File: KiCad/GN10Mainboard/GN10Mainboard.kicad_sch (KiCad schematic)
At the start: 140 parts, among them J1 XT30PW-M, J10 USB_C_Receptacle_USB2.0, J12 Conn_01x04, J4 Conn_01x04, J5 Conn_01x06, J6 Conn_01x04, J7 Conn_01x04, J8 Conn_01x04, J9 RJ45_Bel_SI-60062-F, SW1 SW_Push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

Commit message: update
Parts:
- L3: value 7.2u -> 6.8u
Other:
- note removed: "Virtual COM port allows communication to both STM32 and ESP32 Port A connects to STM, port B to ESP Refer to datasheet for details"
- moved on the sheet: C1, C10, C11, C19, C20, C21, C22, C23, C24, C25, C28, C29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

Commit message: add:footprint
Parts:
- C1, C13, C14, C15: footprint (none) -> Capacitor_SMD:C_0402_1005Metric
- C16, C17, C18, C2, C26: footprint (none) -> Capacitor_SMD:C_1210_3225Metric
- D2: footprint (none) -> Diode_SMD:D_SMC
- JP1, JP2: footprint (none) -> Jumper:SolderJumper-2_P1.3mm_Open_RoundedPad1.0x1.5mm
- L3: footprint (none) -> Inductor_SMD:L_Bourns_SRR1210A
- R11, R12, R13, R14, R2, R3, R4, R40, R41, R42, R43: footprint (none) -> Resistor_SMD:R_0402_1005Metric
- U3: footprint (none) -> Package_SO:SOIC-8_3.9x4.9mm_P1.27mm
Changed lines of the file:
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@@
 			)
 		)
-		(property "Footprint" ""
+		(property "Footprint" "Resistor_SMD:R_0402_1005Metric"
 			(at 88.392 350.52 90)
 			(effects
@@
 			)
 		)
-		(property "Footprint" ""
+		(property "Footprint" "Jumper:SolderJumper-2_P1.3mm_Open_RoundedPad1.0x1.5mm"
 			(at 203.2 293.37 0)
 			(effects
@@
 			)
 		)
-		(property "Footprint" ""
+		(property "Footprint" "Resistor_SMD:R_0402_1005Metric"
 			(at 257.302 73.66 90)
 			(effects
@@
 			)
 		)
-		(property "Footprint" ""
+		(property "Footprint" "Resistor_SMD:R_0402_1005Metric"
 			(at 159.512 80.01 90)
 			(effects
@@
 			)
 		)
-		(property "Footprint" ""
+		(property "Footprint" "Resistor_SMD:R_0402_1005Metric"
 			(at 257.302 85.09 90)
 			(effects
@@
 			)
 		)
-		(property "Footprint" ""
+		(property "Footprint" "Package_SO:SOIC-8_3.9x4.9mm_P1.27mm"
 			(at 74.93 361.95 0)
 			(effects
@@
 			)
 		)
-		(property "Footprint" ""
+		(property "Footprint" "Resistor_SMD:R_0402_1005Metric"
 			(at 96.012 350.52 90)
 			(effects
@@
 			)
 		)
-		(property "Footprint" ""
+		(property "Footprint" "Resistor_SMD:R_0402_1005Metric"
 			(at 103.632 350.52 90)
 			(effects
@@
 			)
 		)
-		(property "Footprint" ""
+		(property "Footprint" "Resistor_SMD:R_0402_1005Metric"
 			(at 121.412 80.01 90)
 			(effects
@@
 			)
 		)
-		(property "Footprint" ""
+		(property "Footprint" "Capacitor_SMD:C_1210_3225Metric"
 			(at 233.3752 74.93 0)
 			(effects
@@
 			)
 		)
-		(property "Footprint" ""
+		(property "Footprint" "Capacitor_SMD:C_1210_3225Metric"
 			(at 97.4852 69.85 0)
 			(effects
@@
 			)
 		)
-		(property "Footprint" ""
+		(property "Footprint" "Diode_SMD:D_SMC"
 			(at 201.93 71.12 0)
 			(effects
@@
 			)
 		)
-		(property "Footprint" ""
+		(property "Footprint" "Inductor_SMD:L_Bourns_SRR1210A"
 			(at 212.09 67.31 0)
 			(effects
@@
 			)
 		)
-		(property "Footprint" ""
+		(property "Footprint" "Capacitor_SMD:C_0402_1005Metric"
 			(at 56.8452 361.95 0)
 			(effects
@@
 			)
 		)
-		(property "Footprint" ""
+		(property "Footprint" "Capacitor_SMD:C_0402_1005Metric"
 			(at 138.1252 81.28 0)
 			(effects
@@
 			)
 		)
-		(property "Footprint" ""
+		(property "Footprint" "Resistor_SMD:R_0402_1005Metric"
 			(at 194.31 295.148 90)
 			(effects
@@
 			)
 		)
-		(property "Footprint" ""
+		(property "Footprint" "Capacitor_SMD:C_1210_3225Metric"
 			(at 244.8052 74.93 0)
 			(effects
@@
 			)
 		)
-		(property "Footprint" ""
+		(property "Footprint" "Capacitor_SMD:C_0402_1005Metric"
 			(at 195.2752 67.31 0)
 			(effects
@@
 			)
 		)
-		(property "Footprint" ""
+		(property "Footprint" "Resistor_SMD:R_0402_1005Metric"
 			(at 121.412 66.04 90)
 			(effects
@@
 			)
 		)
-		(property "Footprint" ""
+		(property "Footprint" "Capacitor_SMD:C_0402_1005Metric"
 			(at 148.2852 85.09 0)
 			(effects
@@
 			)
 		)
-		(property "Footprint" ""
+		(property "Footprint" "Jumper:SolderJumper-2_P1.3mm_Open_RoundedPad1.0x1.5mm"
 			(at 203.2 290.83 0)
 			(effects
@@
 			)
 		)
-		(property "Footprint" ""
+		(property "Footprint" "Resistor_SMD:R_0402_1005Metric"
 			(at 145.542 73.66 90)
 			(effects
@@
 			)
 		)
-		(property "Footprint" ""
+		(property "Footprint" "Capacitor_SMD:C_1210_3225Metric"
 			(at 108.9152 69.85 0)
 			(effects
@@
 			)
 		)
-		(property "Footprint" ""
+		(property "Footprint" "Capacitor_SMD:C_1210_3225Metric"
 			(at 221.9452 74.93 0)
 			(effects
@@
 			)
 		)
-		(property "Footprint" ""
+		(property "Footprint" "Resistor_SMD:R_0402_1005Metric"
 			(at 101.6 366.268 90)
 			(effects

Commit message: update
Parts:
- added J11, J2, J3: Conn_01x04, Connector_JST:JST_XH_B4B-XH-A_1x04_P2.50mm_Vertical, symbol Connector_Generic:Conn_01x04
- added J13, J14: Conn_01x06, Connector_JST:JST_XH_B6B-XH-A_1x06_P2.50mm_Vertical, symbol Connector_Generic:Conn_01x06
- added R44, R45, R46: 120, Resistor_SMD:R_0402_1005Metric, symbol Device:R
- R43: value 330 -> 470
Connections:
- net +3.3V: now also J13.2 (Pin_2), J14.2 (Pin_2)
- net +5V: now also J11.3 (Pin_3), J2.3 (Pin_3), J3.3 (Pin_3)
- net CAN1_H: now also J2.4 (Pin_4), R44.1
- net CAN1_L: now also J2.2 (Pin_2), R44.2
- net CAN2_H: now also J3.4 (Pin_4), R45.1
- net CAN2_L: now also J3.2 (Pin_2), R45.2
- net CAN3_H: now also J11.4 (Pin_4), R46.1
- net CAN3_L: now also J11.2 (Pin_2), R46.2
- net GND: now also J11.1 (Pin_1), J13.4 (Pin_4), J14.4 (Pin_4), J2.1 (Pin_1), J3.1 (Pin_1)
- net TIM3_CH1: now also J14.1 (Pin_1); no longer J5.6 (Pin_6)
- net TIM3_CH2: now also J14.3 (Pin_3); no longer J5.5 (Pin_5)
- net TIM2_CH1: now reaches U4.12 (PA0)
- net TIM2_CH1: now also J13.1 (Pin_1)
- net TIM2_CH2: now reaches U4.13 (PA1)
- net TIM2_CH2: now also J13.3 (Pin_3)
- no-connect marks 53 -> 57
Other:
- note added: "+5V max current : 5A"
- note added: "BATT : 7.2-24V"
- note added: "Switch"
- note removed: "BATT : 7-14V"
- note removed: "External-Switch"
- moved on the sheet: C13, C14, C15, C16, C17, C18, C19, C2, C20, C21, C22, C23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

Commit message: add:Jetson connectors
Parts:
- added C27, C41: 0.1u, Capacitor_SMD:C_0402_1005Metric, symbol Device:C
- added D8: White, LED_SMD:LED_0603_1608Metric, symbol Device:LED
- added J15: Conn_01x12, symbol Connector_Generic:Conn_01x12
- added J16: Conn_01x04, symbol Connector_Generic:Conn_01x04
- added J17: Conn_01x04, Connector_JST:JST_XH_B4B-XH-A_1x04_P2.50mm_Vertical, symbol Connector_Generic:Conn_01x04
- added JP3, JP4: Jumper_2_Small_Open, Jumper:SolderJumper-2_P1.3mm_Open_RoundedPad1.0x1.5mm, symbol Jumper:Jumper_2_Small_Open
- added R47: 120, Resistor_SMD:R_0402_1005Metric, symbol Device:R
- added U11: MCP2562-E-SN, Package_SO:SOIC-8_3.9x4.9mm_P1.27mm, symbol Interface_CAN_LIN:MCP2562-E-SN
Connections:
- net +5V: now also C41.1, J17.3 (Pin_3), U11.3 (VDD)
- net GND: now also C27.2, C41.2, J15.11 (Pin_11), J15.7 (Pin_7), J15.9 (Pin_9), J16.3 (Pin_3), J17.1 (Pin_1), U11.2 (VSS), U11.8 (STBY)
- net SYS_SWDIO: now also U9.18 (ADBUS2)
- net at JP2.1 (A), R43.1: now also JP4.1 (A); no longer U9.18 (ADBUS2)
- net at JP1.1 (A), U9.16 (ADBUS0): now also JP3.1 (A)
- new net JETSON_3.3V: C27.1, J16.4 (Pin_4), U11.5 (Vio)
- new net JETSON_CAN_H: J17.4 (Pin_4), R47.1, U11.7 (CANH)
- new net JETSON_CAN_L: J17.2 (Pin_2), R47.2, U11.6 (CANL)
- new net JETSON_CAN_RX: J16.2 (Pin_2), U11.4 (RXD)
- new net JETSON_CAN_TX: J16.1 (Pin_1), U11.1 (TXD)
- new net JETSON_PC_LED+: D8.2 (A), J15.2 (Pin_2)
- new net JETSON_PC_LED-: D8.1 (K), J15.1 (Pin_1)
- new net JETSON_UART2_RXD: J15.3 (Pin_3), JP4.2 (B)
- new net JETSON_UART2_TXD: J15.4 (Pin_4), JP3.2 (B)
- no-connect marks 57 -> 62
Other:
- moved on the sheet: JP1, JP2

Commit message: remove:jetson connectors
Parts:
- removed C27, C41: 0.1u, Capacitor_SMD:C_0402_1005Metric, symbol Device:C
- removed D8: White, LED_SMD:LED_0603_1608Metric, symbol Device:LED
- removed J15: Conn_01x12, symbol Connector_Generic:Conn_01x12
- removed J16: Conn_01x04, symbol Connector_Generic:Conn_01x04
- removed J17: Conn_01x04, Connector_JST:JST_XH_B4B-XH-A_1x04_P2.50mm_Vertical, symbol Connector_Generic:Conn_01x04
- removed JP3, JP4: Jumper_2_Small_Open, Jumper:SolderJumper-2_P1.3mm_Open_RoundedPad1.0x1.5mm, symbol Jumper:Jumper_2_Small_Open
- removed R47: 120, Resistor_SMD:R_0402_1005Metric, symbol Device:R
- removed U11: MCP2562-E-SN, Package_SO:SOIC-8_3.9x4.9mm_P1.27mm, symbol Interface_CAN_LIN:MCP2562-E-SN
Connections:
- net SYS_SWDIO: no longer U9.18 (ADBUS2)
- net at JP2.1 (A), R43.1: now also U9.18 (ADBUS2)
- no-connect marks 62 -> 57

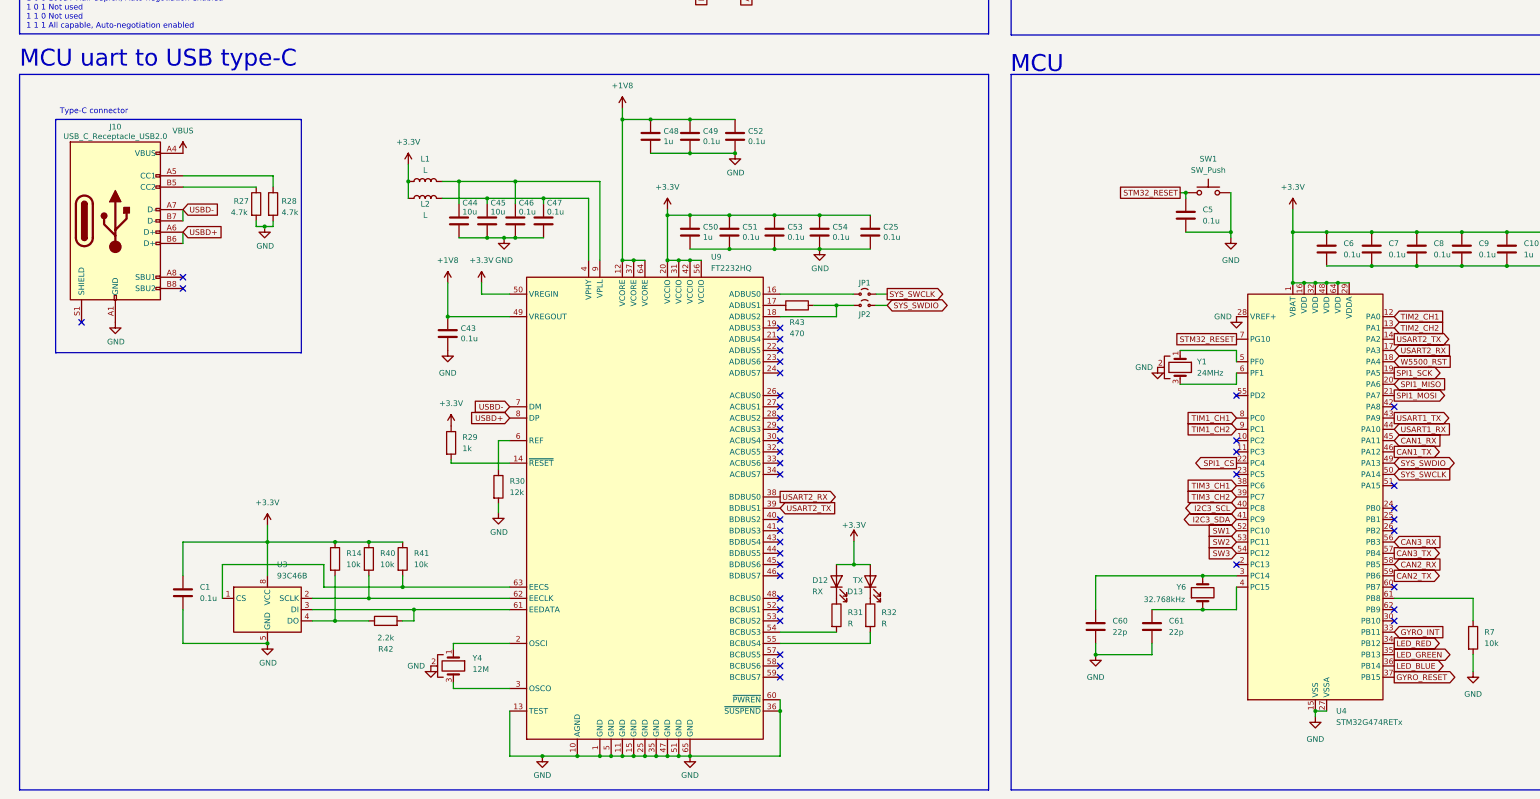
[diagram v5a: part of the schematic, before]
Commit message: update:Serial conv to ft231xs
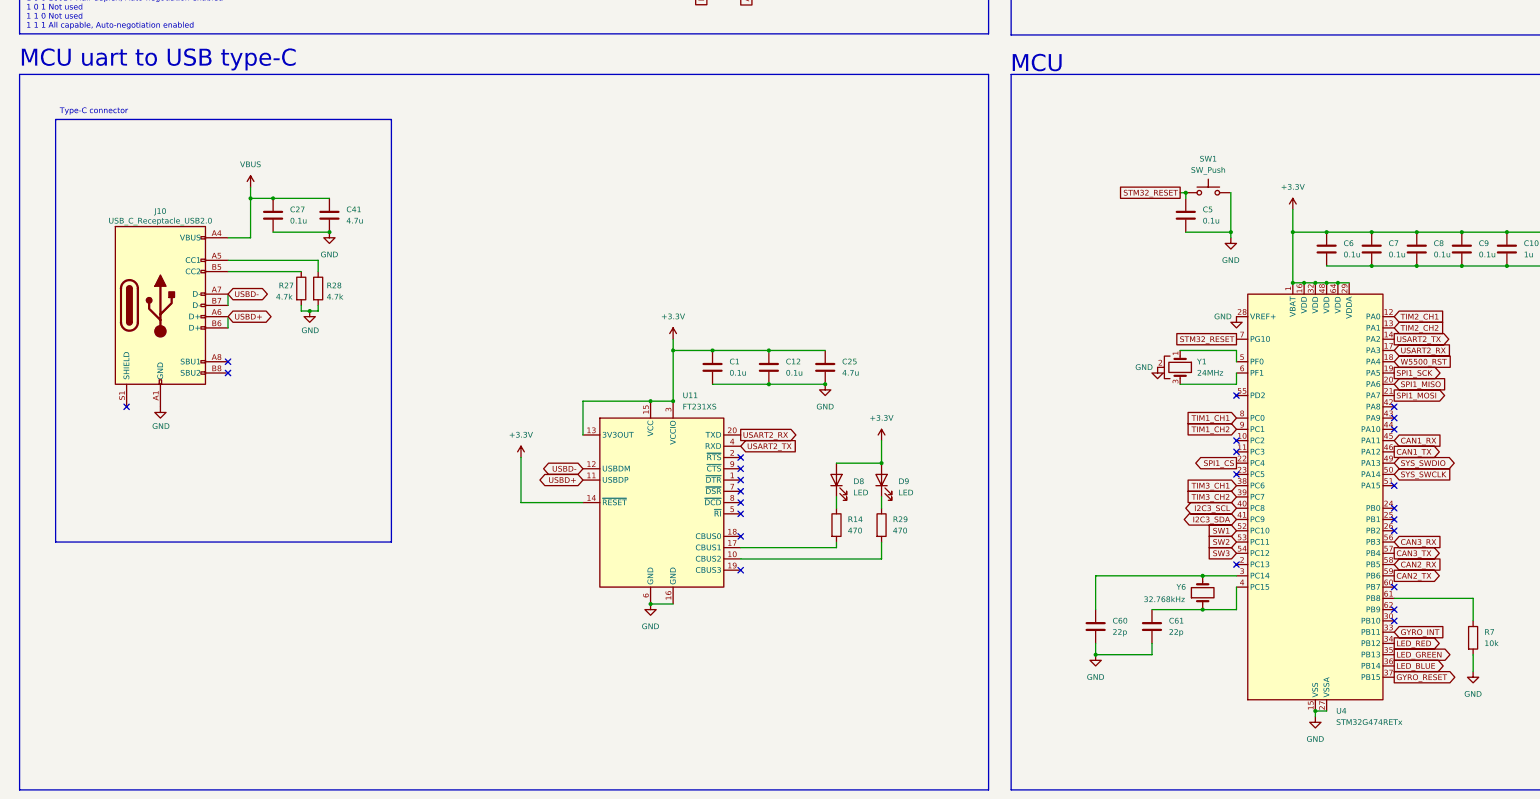
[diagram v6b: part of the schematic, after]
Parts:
- removed C43, C46, C47, C49, C51, C52, C53, C54: 0.1u, Capacitor_SMD:C_0402_1005Metric, symbol Device:C
- removed C44, C45: 10u, Resistor_SMD:R_0603_1608Metric, symbol Device:C
- removed C48, C50: 1u, Capacitor_SMD:C_0402_1005Metric, symbol Device:C
- removed D12: RX, LED_SMD:LED_0603_1608Metric, symbol Device:LED
- removed D13: TX, LED_SMD:LED_0603_1608Metric, symbol Device:LED
- removed JP1, JP2: Jumper_2_Small_Open, Jumper:SolderJumper-2_P1.3mm_Open_RoundedPad1.0x1.5mm, symbol Jumper:Jumper_2_Small_Open
- removed L1, L2: L, Inductor_SMD:L_0603_1608Metric, symbol Device:L
- removed R30: 12k, Resistor_SMD:R_0402_1005Metric, symbol Device:R
- removed R31, R32: R, Resistor_SMD:R_0402_1005Metric, symbol Device:R
- removed R40, R41: 10k, Resistor_SMD:R_0402_1005Metric, symbol Device:R
- removed R42: 2.2k, Resistor_SMD:R_0402_1005Metric, symbol Device:R
- removed R43: 470, Resistor_SMD:R_0402_1005Metric, symbol Device:R
- removed U3: 93C46B, Package_SO:SOIC-8_3.9x4.9mm_P1.27mm, symbol Memory_EEPROM:93CxxB
- removed U9: FT2232HQ, Package_DFN_QFN:QFN-64-1EP_9x9mm_P0.5mm_EP4.35x4.35mm, symbol Interface_USB:FT2232HQ
- removed Y4: 12M, Crystal:Resonator_SMD_Murata_CSTxExxV-3Pin_3.0x1.1mm, symbol Device:Crystal_GND2
- added C12, C27: 0.1u, symbol Device:C
- added C41: 4.7u, symbol Device:C
- added D8, D9: LED, symbol Device:LED
- added U11: FT231XS, Package_SO:SSOP-20_3.9x8.7mm_P0.635mm, symbol Interface_USB:FT231XS
- C1: footprint Capacitor_SMD:C_0402_1005Metric -> (none)
- C25: value 0.1u -> 4.7u; footprint Capacitor_SMD:C_0402_1005Metric -> (none)
- R14: value 10k -> 470; footprint Resistor_SMD:R_0402_1005Metric -> (none)
- R29: value 1k -> 470; footprint Resistor_SMD:R_0402_1005Metric -> (none)
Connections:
- net +3.3V: now also C12.1, D8.2 (A), D9.2 (A), U11.13 (3V3OUT), U11.14 (~{RESET}), U11.15 (VCC), U11.3 (VCCIO); no longer R14.1, R29.1
- net GND: now also C12.2, C27.2, C41.2, U11.16 (GND), U11.6 (GND)
- net USART2_RX: now also U11.20 (TXD)
- net USART2_TX: now also U11.4 (RXD)
- net USBD+: now also U11.11 (USBDP)
- net USBD-: now also U11.12 (USBDM)
- net VBUS: now also C27.1, C41.1
- net at R14.2: now also U11.17 (CBUS1)
- net at R29.2: now also U11.10 (CBUS2)
- net USART1_RX: no longer names the net of U4.44 (PA10)
- net USART1_TX: no longer names the net of U4.43 (PA9)
- new net: D9.1 (K), R29.1
- new net: D8.1 (K), R14.1
- no-connect marks 57 -> 42
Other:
- moved on the sheet: J10, R27, R28

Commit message: add:footprint to serial-conv
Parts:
- C1, C12, C27: footprint (none) -> Capacitor_SMD:C_0402_1005Metric
- C25, C41: footprint (none) -> Capacitor_SMD:C_0603_1608Metric
- D8, D9: footprint (none) -> LED_SMD:LED_0603_1608Metric
- R14, R29: footprint (none) -> Resistor_SMD:R_0402_1005Metric
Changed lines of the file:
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@@
 			)
 		)
-		(property "Footprint" ""
+		(property "Footprint" "LED_SMD:LED_0603_1608Metric"
 			(at 213.36 332.74 0)
 			(effects
@@
 			)
 		)
-		(property "Footprint" ""
+		(property "Footprint" "Capacitor_SMD:C_0402_1005Metric"
 			(at 188.9252 311.15 0)
 			(effects
@@
 			)
 		)
-		(property "Footprint" ""
+		(property "Footprint" "Capacitor_SMD:C_0402_1005Metric"
 			(at 176.2252 311.15 0)
 			(effects
@@
 			)
 		)
-		(property "Footprint" ""
+		(property "Footprint" "Capacitor_SMD:C_0603_1608Metric"
 			(at 89.8652 276.86 0)
 			(effects
@@
 			)
 		)
-		(property "Footprint" ""
+		(property "Footprint" "Resistor_SMD:R_0402_1005Metric"
 			(at 211.582 342.9 90)
 			(effects
@@
 			)
 		)
-		(property "Footprint" ""
+		(property "Footprint" "Resistor_SMD:R_0402_1005Metric"
 			(at 201.422 342.9 90)
 			(effects
@@
 			)
 		)
-		(property "Footprint" ""
+		(property "Footprint" "Capacitor_SMD:C_0603_1608Metric"
 			(at 201.6252 311.15 0)
 			(effects
@@
 			)
 		)
-		(property "Footprint" ""
+		(property "Footprint" "Capacitor_SMD:C_0402_1005Metric"
 			(at 77.1652 276.86 0)
 			(effects
@@
 			)
 		)
-		(property "Footprint" ""
+		(property "Footprint" "LED_SMD:LED_0603_1608Metric"
 			(at 203.2 332.74 0)
 			(effects

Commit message: update:PCB
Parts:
- removed J11, J2, J3: Conn_01x04, Connector_JST:JST_XH_B4B-XH-A_1x04_P2.50mm_Vertical, symbol Connector_Generic:Conn_01x04
